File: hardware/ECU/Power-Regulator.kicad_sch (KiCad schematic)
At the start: 22 parts, among them Q3 Q_PNP_BCEC, U15 MC33814, U16 TC4424A

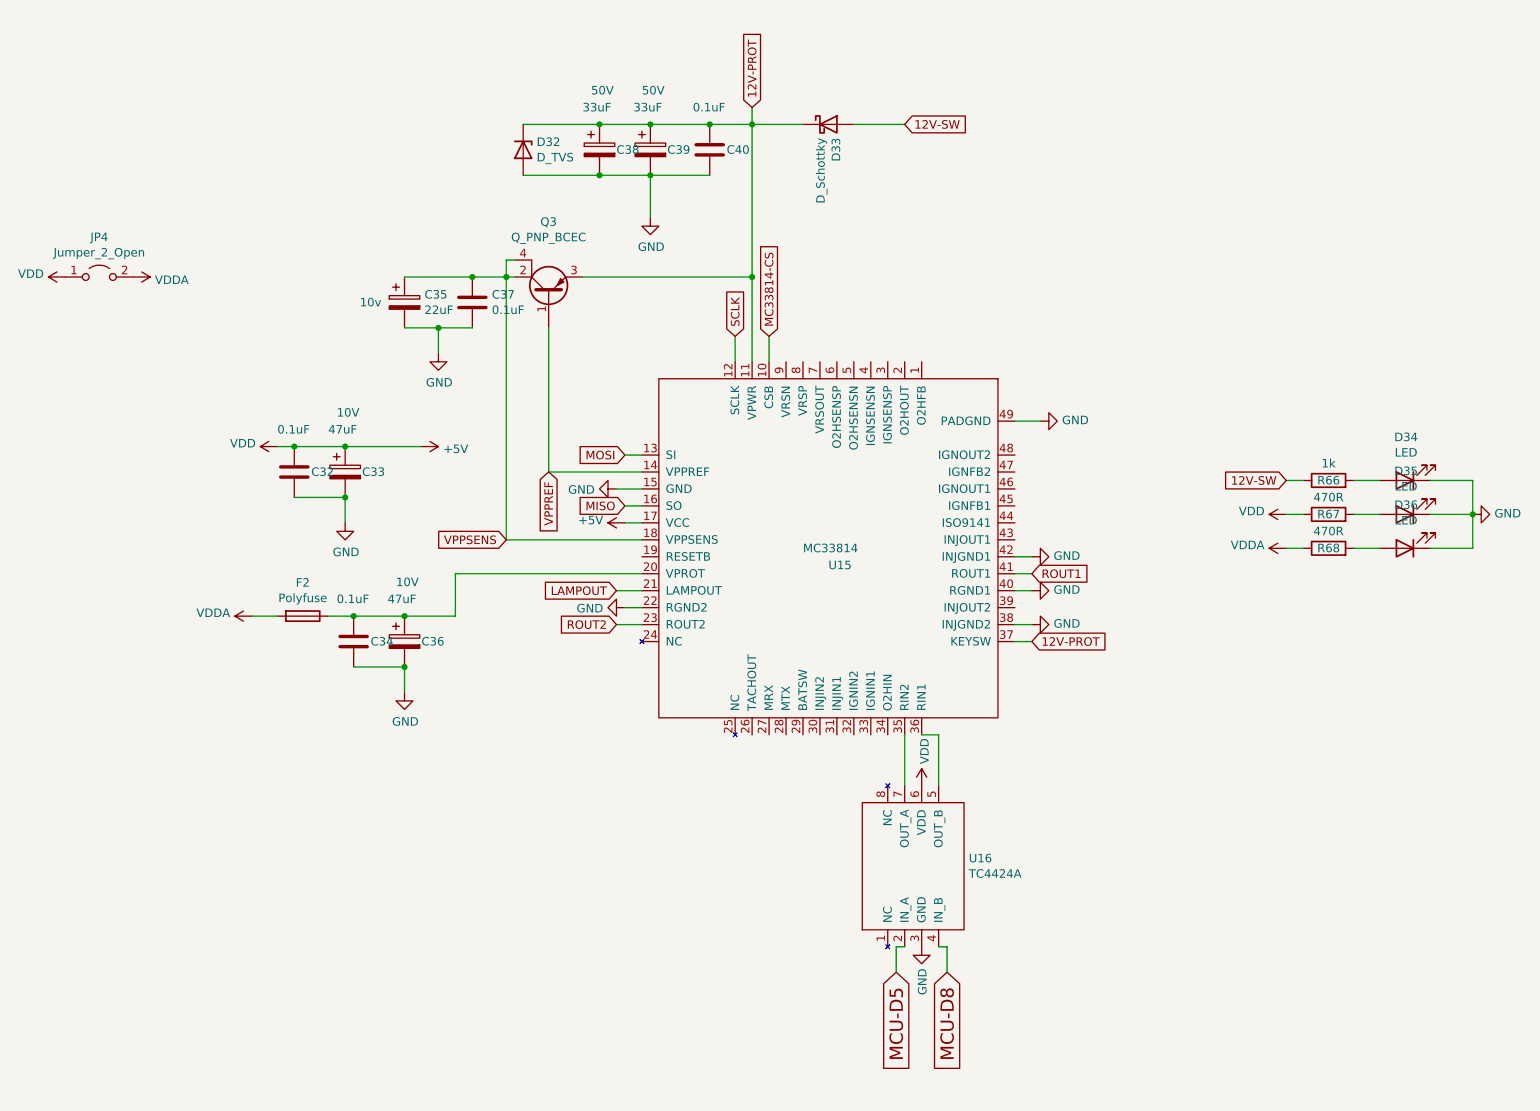
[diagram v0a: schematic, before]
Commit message: Replace speeduino submodule with HasiKe fork, fix teensy.pretty path
- Switch speeduino from speeduino/speeduino to HasiKe/speeduino
- Fix teensy.pretty submodule path case mismatch (Hardware -> hardware)
- Add ISL9V5036P3-F085 component library
- Various ECU schematic updates
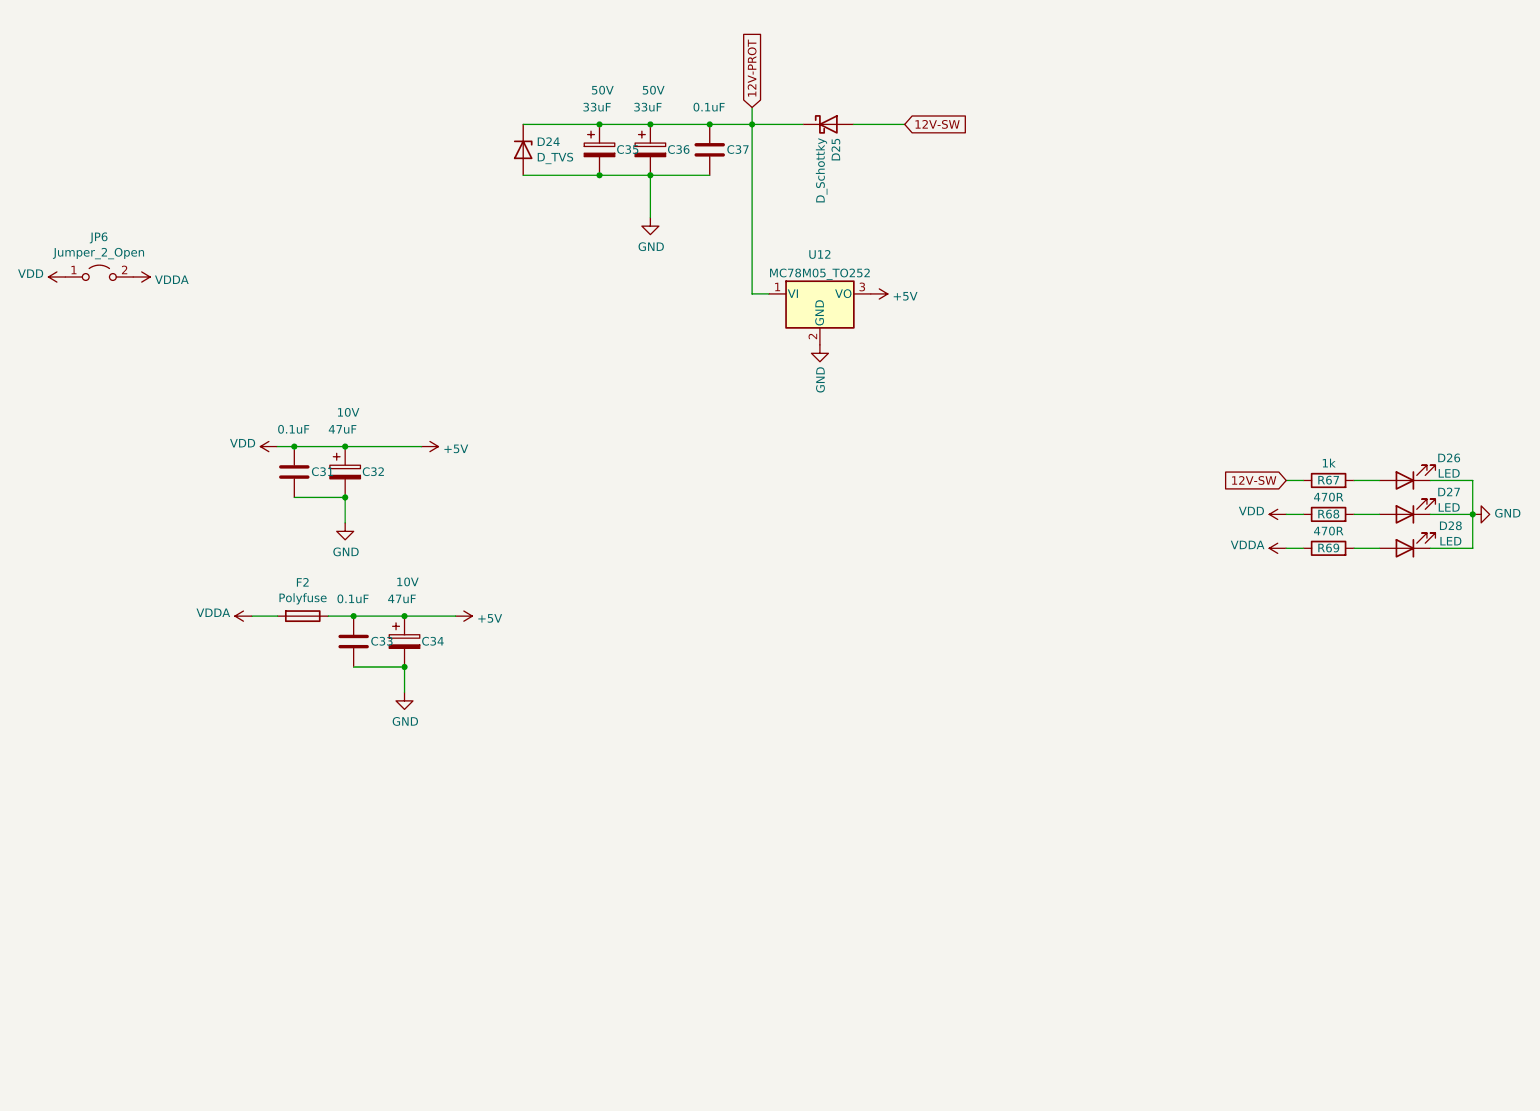
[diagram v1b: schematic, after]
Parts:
- removed C35: 22uF, Capacitor_SMD:CP_Elec_4x5.4, symbol Device:CP
- removed C37: 0.1uF, Capacitor_SMD:C_0805_2012Metric, symbol Device:C
- removed Q3: Q_PNP_BCEC, Package_TO_SOT_SMD:SOT-223-3_TabPin2, symbol Device:Q_PNP_BCEC
- removed U15: MC33814, Package_QFP:LQFP-48-1EP_7x7mm_P0.5mm_EP3.6x3.6mm_ThermalVias, symbol IC_Automotive:MC33814
- removed U16: TC4424A, Package_SO:SOIC-8_3.9x4.9mm_P1.27mm, symbol IC_Automotive:TC4424A
- added U12: MC78M05_TO252, Package_TO_SOT_SMD:TO-252-2, symbol Regulator_Linear:MC78M05_TO252
- renumbered C32 to C31, C33 to C32, C34 to C33, C36 to C34, C38 to C35, C39 to C36, C40 to C37, D32 to D24, D33 to D25, D34 to D26, D35 to D27, D36 to D28, JP4 to JP6, R66 to R67, R67 to R68, R68 to R69
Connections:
- net +5V: now also C33.1, C34.1, F2.1, U12.3 (VO)
- net 12V-PROT: now also U12.1 (VI)
- net GND: now also U12.2 (GND)
